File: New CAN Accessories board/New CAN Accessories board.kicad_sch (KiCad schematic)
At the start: 19 parts, among them J10 39301040, J11 ATF13-2P-BM03, J12 Conn_01x02_Pin, J13 Conn_01x12_Pin, J14 Conn_01x08_Pin, J9 39301060, T1 MCP2562FD-E_SN, U1 NUCLEO_L432KC

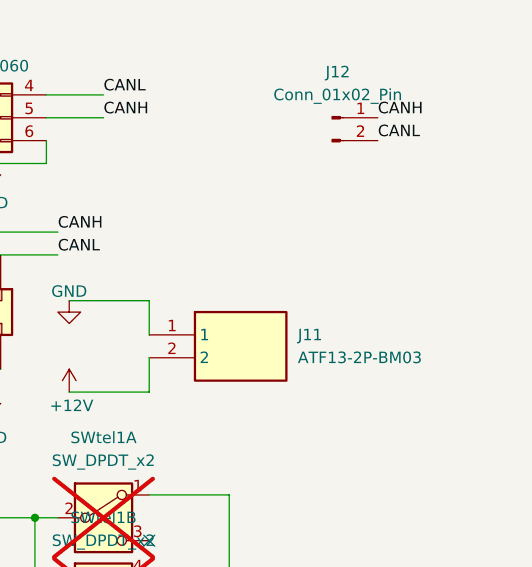
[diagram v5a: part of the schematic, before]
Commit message: added bulk cap
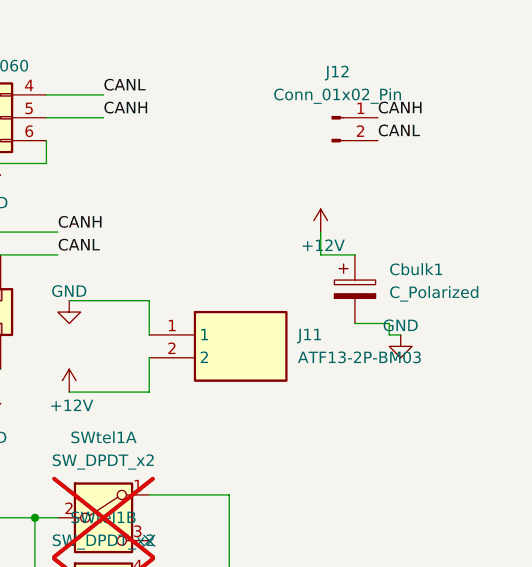
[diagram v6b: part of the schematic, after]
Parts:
- added Cbulk1: C_Polarized, symbol Device:C_Polarized
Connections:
- net +12V: now also Cbulk1.1
- net GND: now also Cbulk1.2
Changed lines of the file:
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@@
 	(wire
 		(pts
+			(xy 204.47 102.87) (xy 200.66 102.87)
+		)
+		(stroke
+			(width 0)
+			(type default)
+		)
+	)
+	(wire
+		(pts
 			(xy 177.8 130.81) (xy 186.69 130.81)
 		)
@@
 	(wire
 		(pts
+			(xy 204.47 104.14) (xy 204.47 102.87)
+		)
+		(stroke
+			(width 0)
+			(type default)
+		)
+	)
+	(wire
+		(pts
 			(xy 68.58 173.99) (xy 76.2 173.99)
 		)
@@
 	(wire
 		(pts
+			(xy 196.85 92.71) (xy 196.85 95.25)
+		)
+		(stroke
+			(width 0)
+			(type default)
+		)
+	)
+	(wire
+		(pts
 			(xy 129.54 140.97) (xy 148.59 140.97)
 		)
@@
 	(wire
 		(pts
+			(xy 196.85 95.25) (xy 200.66 95.25)
+		)
+		(stroke
+			(width 0)
+			(type default)
+		)
+	)
+	(wire
+		(pts
 			(xy 177.8 121.92) (xy 186.69 121.92)
 		)
@@
 	(wire
 		(pts
+			(xy 205.74 104.14) (xy 204.47 104.14)
+		)
+		(stroke
+			(width 0)
+			(type default)
+		)
+	)
+	(wire
+		(pts
 			(xy 177.8 110.49) (xy 177.8 106.68)
 		)
@@
 	)
 	(symbol
+		(lib_id "power:+12V")
+		(at 196.85 92.71 0)
+		(unit 1)
+		(exclude_from_sim no)
+		(in_bom yes)
+		(on_board yes)
+		(dnp no)
+		(property "Reference" "#PWR036"
+			(at 196.85 96.52 0)
+			(effects
+				(font
+					(size 1.27 1.27)
+				)
+				(hide yes)
+			)
+		)
+		(property "Value" "+12V"
+			(at 197.104 94.234 0)
+			(effects
+				(font
+					(size 1.27 1.27)
+				)
+			)
+		)
+		(property "Footprint" ""
+			(at 196.85 92.71 0)
+			(effects
+				(font
+					(size 1.27 1.27)
+				)
+				(hide yes)
+			)
+		)
+		(property "Datasheet" ""
+			(at 196.85 92.71 0)
+			(effects
+				(font
+					(size 1.27 1.27)
+				)
+				(hide yes)
+			)
+		)
+		(property "Description" ""
+			(at 196.85 92.71 0)
+			(effects
+				(font
+					(size 1.27 1.27)
+				)
+			)
+		)
+		(pin "1"
+		)
+		(instances
+			(project "New CAN Accessories board"
+				(path "/88340f43-3f46-45a6-9393-130e00dc3071"
+					(reference "#PWR036")
+					(unit 1)
+				)
+			)
+		)
+	)
+	(symbol
 		(lib_id "power:GND")
 		(at 168.91 100.33 0)
@@
 	)
 	(symbol
+		(lib_id "power:GND")
+		(at 205.74 104.14 0)
+		(unit 1)
+		(exclude_from_sim no)
+		(in_bom yes)
+		(on_board yes)
+		(dnp no)
+		(property "Reference" "#PWR037"
+			(at 205.74 110.49 0)
+			(effects
+				(font
+					(size 1.27 1.27)
+				)
+				(hide yes)
+			)
+		)
+		(property "Value" "GND"
+			(at 205.74 103.124 0)
+			(effects
+				(font
+					(size 1.27 1.27)
+				)
+			)
+		)
+		(property "Footprint" ""
+			(at 205.74 104.14 0)
+			(effects
+				(font
+					(size 1.27 1.27)
+				)
+				(hide yes)
+			)
+		)
+		(property "Datasheet" ""
+			(at 205.74 104.14 0)
+			(effects
+				(font
+					(size 1.27 1.27)
+				)
+				(hide yes)
+			)
+		)
+		(property "Description" "Power symbol creates a global label with name \"GND\" , ground"
+			(at 205.74 104.14 0)
+			(effects
+				(font
+					(size 1.27 1.27)
+				)
+				(hide yes)
+			)
+		)
+		(pin "1"
+		)
+		(instances
+			(project "New CAN Accessories board"
+				(path "/88340f43-3f46-45a6-9393-130e00dc3071"
+					(reference "#PWR037")
+					(unit 1)
+				)
+			)
+		)
+	)
+	(symbol
 		(lib_id "Device:R")
 		(at 129.54 146.05 0)
@@
 					(unit 1)
 				)
+			)
+		)
+	)
+	(symbol
+		(lib_id "Device:C_Polarized")
+		(at 200.66 99.06 0)
+		(unit 1)
+		(exclude_from_sim no)
+		(in_bom yes)
+		(on_board yes)
+		(dnp no)
+		(fields_autoplaced yes)
+		(property "Reference" "Cbulk1"
+			(at 204.47 96.9009 0)
+			(effects
+				(font
+					(size 1.27 1.27)
+				)
+				(justify left)
+			)
+		)
+		(property "Value" "C_Polarized"
+			(at 204.47 99.4409 0)
+			(effects
+				(font
+					(size 1.27 1.27)
+				)
+				(justify left)
+			)
+		)
+		(property "Footprint" ""
+			(at 201.6252 102.87 0)
+			(effects
+				(font
+					(size 1.27 1.27)
+				)
+				(hide yes)
+			)
+		)
+		(property "Datasheet" "~"
+			(at 200.66 99.06 0)
+			(effects
+				(font
+					(size 1.27 1.27)
+				)
+				(hide yes)
+			)
+		)
+		(property "Description" "Polarized capacitor"
+			(at 200.66 99.06 0)
+			(effects
+				(font
+					(size 1.27 1.27)
+				)
+				(hide yes)
+			)
+		)
+		(pin "1"
+		)
+		(pin "2"
+		)
+		(instances
+			(project ""
+				(path "/88340f43-3f46-45a6-9393-130e00dc3071"
+					(reference "Cbulk1")
+					(unit 1)
+				)

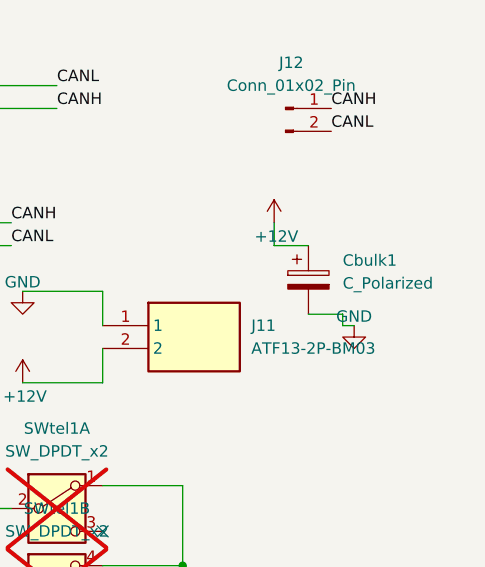
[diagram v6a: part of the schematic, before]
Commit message: added bulk cap
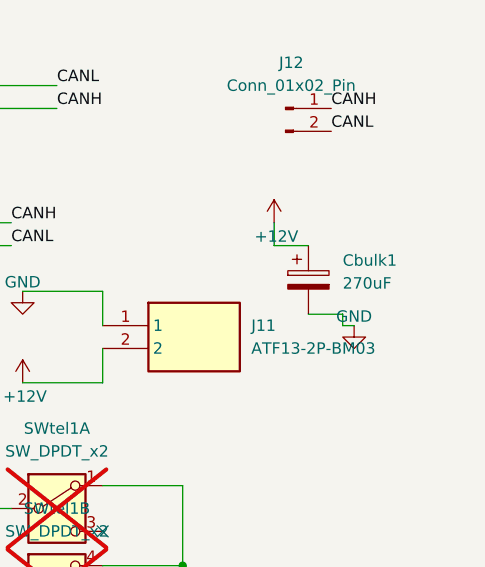
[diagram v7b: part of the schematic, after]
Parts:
- Cbulk1: value C_Polarized -> 270uF; footprint (none) -> footprint:CAPAE1030X1050M
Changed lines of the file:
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@@
 			)
 		)
-		(property "Value" "C_Polarized"
+		(property "Value" "270uF"
 			(at 204.47 99.4409 0)
 			(effects
@@
 			)
 		)
-		(property "Footprint" ""
+		(property "Footprint" "footprint:CAPAE1030X1050M"
 			(at 201.6252 102.87 0)
 			(effects

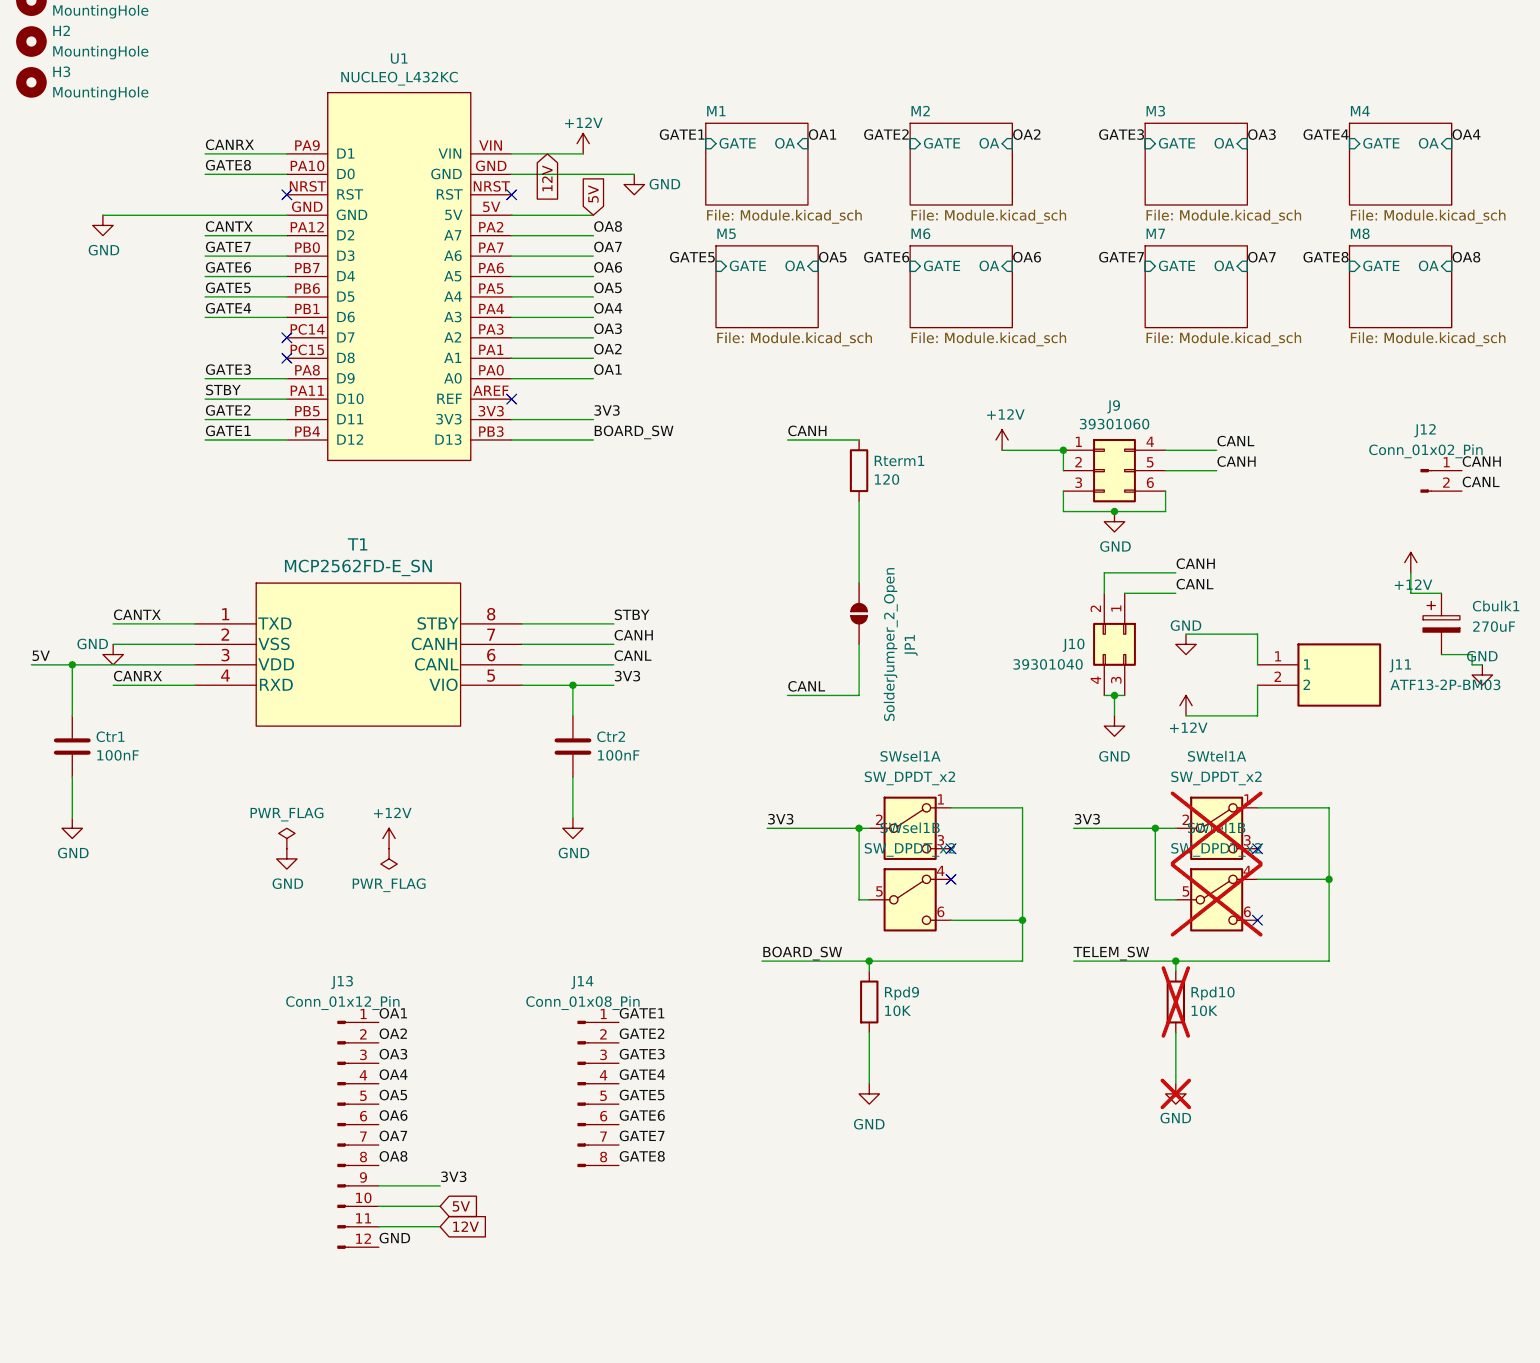
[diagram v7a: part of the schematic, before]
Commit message: Added two 1x4 pin headers for J1-J8 - also fixed CAN module
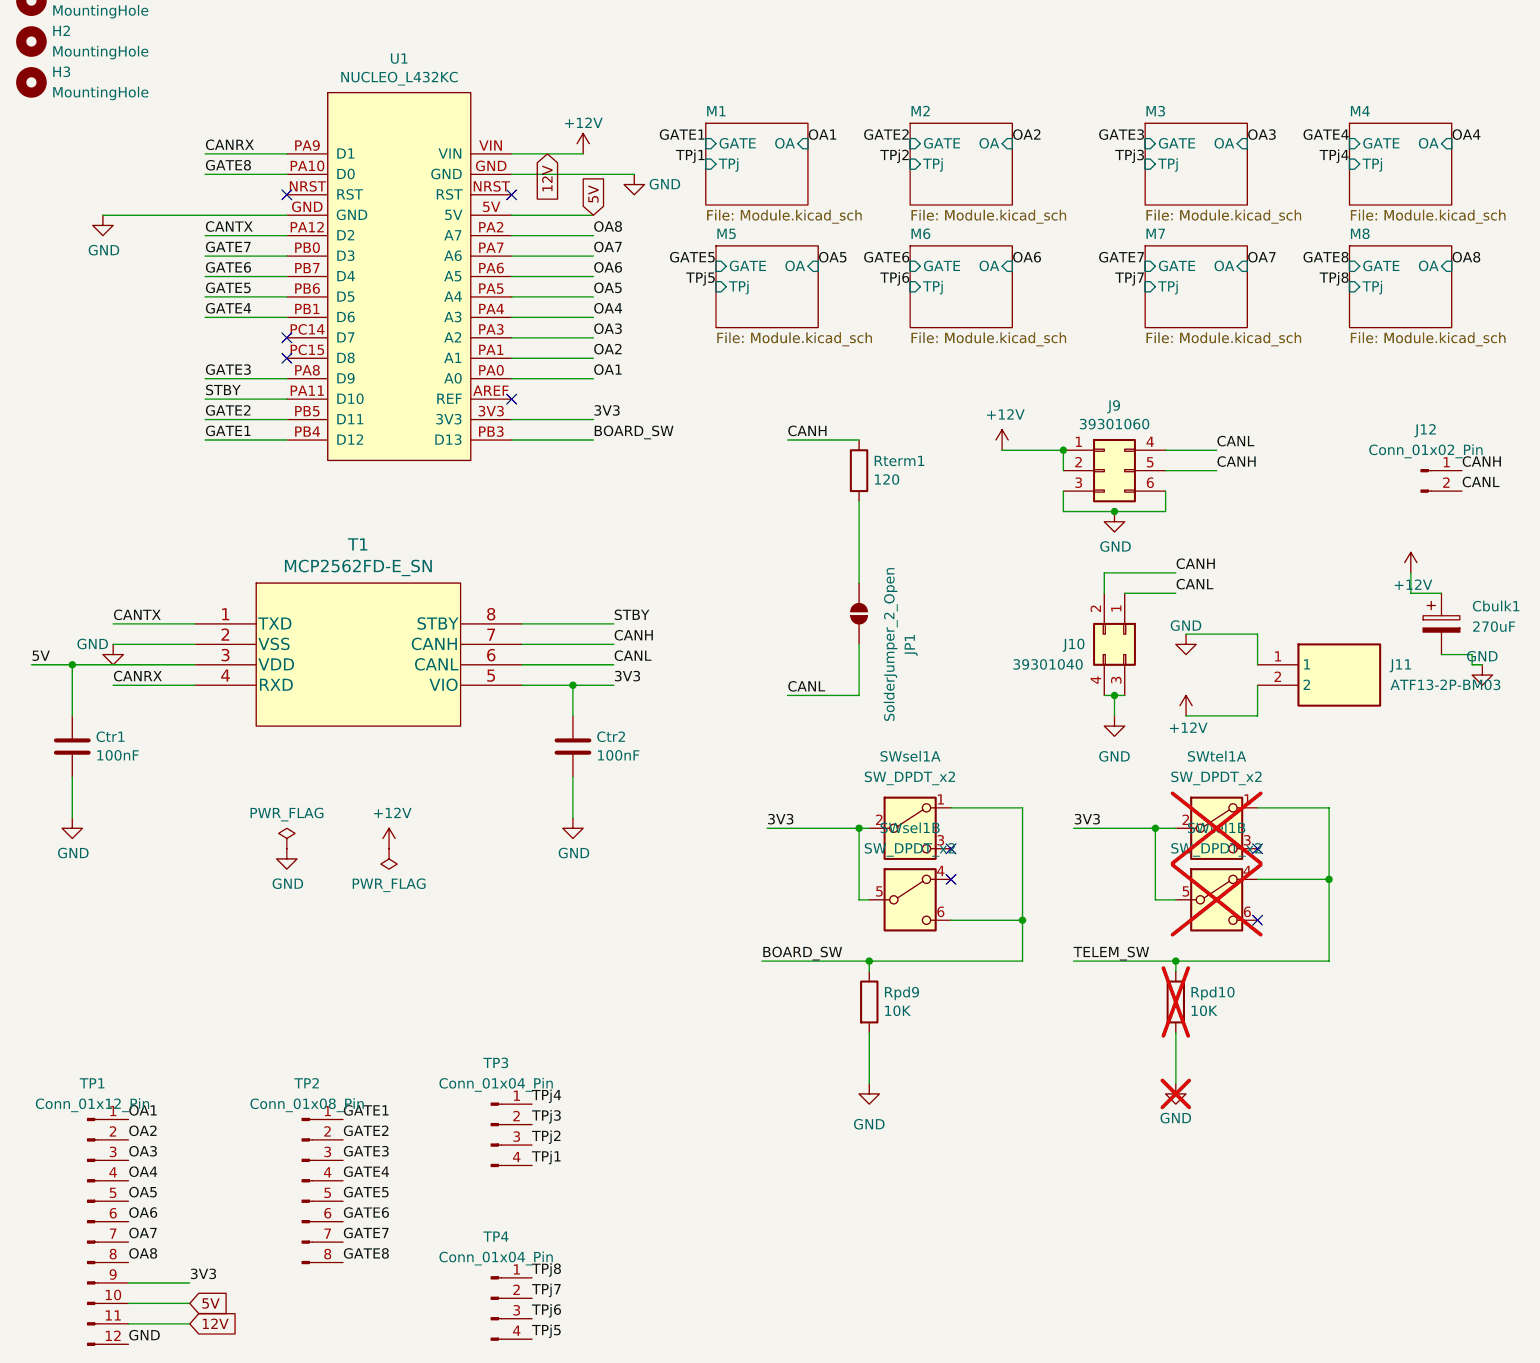
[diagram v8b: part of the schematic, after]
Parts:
- added TP3, TP4: Conn_01x04_Pin, Connector_PinHeader_2.54mm:PinHeader_1x04_P2.54mm_Vertical, symbol Connector:Conn_01x04_Pin
- renumbered J13 to TP1, J14 to TP2
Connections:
- new net TPj1: TP3.4 (Pin_4)
- new net TPj2: TP3.3 (Pin_3)
- new net TPj3: TP3.2 (Pin_2)
- new net TPj4: TP3.1 (Pin_1)
- new net TPj5: TP4.4 (Pin_4)
- new net TPj6: TP4.3 (Pin_3)
- new net TPj7: TP4.2 (Pin_2)
- new net TPj8: TP4.1 (Pin_1)
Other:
- sheet M1 ports: added TPj; removed none
- sheet M2 ports: added TPj; removed none
- sheet M3 ports: added TPj; removed none
- sheet M4 ports: added TPj; removed none
- sheet M5 ports: added TPj; removed none
- sheet M6 ports: added TPj; removed none
- sheet M7 ports: added TPj; removed none
- sheet M8 ports: added TPj; removed none
- moved on the sheet: TP1, TP2
